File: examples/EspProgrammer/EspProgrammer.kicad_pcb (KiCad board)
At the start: 2 copper layers, 35 x 12 mm, 27 parts

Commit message: wip
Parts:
- moved UR5 10.0 mm to (137.5, 60.0), turned to -90 degrees
- moved UR4 8.08 mm to (137.5, 63.0), turned to 90 degrees
- moved UQ2 5.97 mm to (140.0, 63.0)
- moved UQ1 4.56 mm to (140.0, 60.0)
- moved UD3 3.51 mm to (152.0, 60.0)
- moved UR6 3.36 mm to (153.0, 63.0)
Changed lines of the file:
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@@
     (attr smd)
     (fp_text reference "UC4" (at 0 -1.16) (layer "F.SilkS")
-        (effects (font (size 1 1) (thickness 0.15)))
+        (effects (font (size 0.8 0.6) (thickness 0.1)))
     )
     (fp_text value "" (at 0 1.16) (layer "F.Fab")
@@
   )
   (footprint "Package_TO_SOT_SMD:SOT-323_SC-70" (layer "F.Cu")
-    (at 141.115 64.42)
+    (at 140 60)
     (descr "SOT-323, SC-70")
     (tags "SOT-323 SC-70")
@@
     (attr smd)
     (fp_text reference "UQ1" (at -0.05 -1.95) (layer "F.SilkS")
-        (effects (font (size 1 1) (thickness 0.15)))
+        (effects (font (size 0.8 0.6) (thickness 0.1)))
     )
     (fp_text value "BC847AW 1E (CBI) - 45V 200mW 100mA 110@2mA,5V 100MHz 600mV@100mA,5mA NPN +150?@(Tj) SOT-323 Bipolar Transistors - BJT ROHS" (at -0.05 2.05) (layer "F.Fab")
@@
     (attr smd)
     (fp_text reference "UR2" (at 0 -1.17 180) (layer "F.SilkS")
-        (effects (font (size 1 1) (thickness 0.15)))
+        (effects (font (size 0.8 0.6) (thickness 0.1)))
     )
     (fp_text value "" (at 0 1.17 180) (layer "F.Fab")
@@
     (property "edg_short_path" "out")
     (fp_text reference "UJ2" (at -1.27 -4.81) (layer "F.SilkS")
-        (effects (font (size 1 1) (thickness 0.15)))
+        (effects (font (size 0.8 0.6) (thickness 0.1)))
     )
     (fp_text value "PinHeader2.54 Shrouded 2x3 (Generic)" (at -1.27 4.81) (layer "F.Fab")
@@
     (attr smd)
     (fp_text reference "UR1" (at 0 -1.17 180) (layer "F.SilkS")
-        (effects (font (size 1 1) (thickness 0.15)))
+        (effects (font (size 0.8 0.6) (thickness 0.1)))
     )
     (fp_text value "" (at 0 1.17 180) (layer "F.Fab")
@@
   )
   (footprint "Resistor_SMD:R_0402_1005Metric" (layer "F.Cu")
-    (at 145.565 63.45)
+    (at 137.5 63 90)
     (descr "Resistor SMD 0402 (1005 Metric), square (rectangular) end terminal, IPC_7351 nominal, (Body size source: IPC-SM-782 page 72, https://www.pcb-3d.com/wordpress/wp-content/uploads/ipc-sm-782a_amendment_1_and_2.pdf), generated with kicad-footprint-generator")
     (tags "resistor")
@@
     (property "edg_short_path" "auto.dtr_res")
     (attr smd)
-    (fp_text reference "UR4" (at 0 -1.17) (layer "F.SilkS")
-        (effects (font (size 1 1) (thickness 0.15)))
-    )
-    (fp_text value "" (at 0 1.17) (layer "F.Fab")
-        (effects (font (size 1 1) (thickness 0.15)))
-    )
-    (fp_text user "${REFERENCE}" (at 0 0) (layer "F.Fab")
+    (fp_text reference "UR4" (at 0 -1.17 90) (layer "F.SilkS")
+        (effects (font (size 0.8 0.6) (thickness 0.1)))
+    )
+    (fp_text value "" (at 0 1.17 90) (layer "F.Fab")
+        (effects (font (size 1 1) (thickness 0.15)))
+    )
+    (fp_text user "${REFERENCE}" (at 0 0 90) (layer "F.Fab")
         (effects (font (size 0.26 0.26) (thickness 0.04)))
     )
@@
     (fp_line (start 0.525 0.27) (end -0.525 0.27)
       (stroke (width 0.1) (type solid)) (layer "F.Fab"))
-    (pad "1" smd roundrect (at -0.51 0) (size 0.54 0.64) (layers "F.Cu" "F.Paste" "F.Mask") (roundrect_rratio 0.25)
+    (pad "1" smd roundrect (at -0.51 0 90) (size 0.54 0.64) (layers "F.Cu" "F.Paste" "F.Mask") (roundrect_rratio 0.25)
       (net 13 "usbconv.dtr"))
-    (pad "2" smd roundrect (at 0.51 0) (size 0.54 0.64) (layers "F.Cu" "F.Paste" "F.Mask") (roundrect_rratio 0.25)
+    (pad "2" smd roundrect (at 0.51 0 90) (size 0.54 0.64) (layers "F.Cu" "F.Paste" "F.Mask") (roundrect_rratio 0.25)
       (net 22 "auto.dtr_res.b"))
     (model "${KICAD6_3DMODEL_DIR}/Resistor_SMD.3dshapes/R_0402_1005Metric.wrl"
@@
     (attr smd)
     (fp_text reference "UC2" (at 0 -1.16 180) (layer "F.SilkS")
-        (effects (font (size 1 1) (thickness 0.15)))
+        (effects (font (size 0.8 0.6) (thickness 0.1)))
     )
     (fp_text value "" (at 0 1.16 180) (layer "F.Fab")
@@
   )
   (footprint "LED_SMD:LED_0603_1608Metric" (layer "F.Cu")
-    (at 151.615 63.49)
+    (at 152 60)
     (descr "LED SMD 0603 (1608 Metric), square (rectangular) end terminal, IPC_7351 nominal, (Body size source: http://www.tortai-tech.com/upload/download/2011102023233369053.pdf), generated with kicad-footprint-generator")
     (tags "LED")
@@
     (attr smd)
     (fp_text reference "UD3" (at 0 -1.43) (layer "F.SilkS")
-        (effects (font (size 1 1) (thickness 0.15)))
+        (effects (font (size 0.8 0.6) (thickness 0.1)))
     )
     (fp_text value "KT-0603R (Hubei KENTO Elec) - Red 615~630nm 1.9~2.2V 0603 Light Emitting Diodes (LED) RoHS" (at 0 1.43) (layer "F.Fab")
@@
     (attr smd)
     (fp_text reference "UC1" (at 0 -1.16 180) (layer "F.SilkS")
-        (effects (font (size 1 1) (thickness 0.15)))
+        (effects (font (size 0.8 0.6) (thickness 0.1)))
     )
     (fp_text value "" (at 0 1.16 180) (layer "F.Fab")
@@
   )
   (footprint "Resistor_SMD:R_0402_1005Metric" (layer "F.Cu")
-    (at 151.575 66.04)
+    (at 153 63)
     (descr "Resistor SMD 0402 (1005 Metric), square (rectangular) end terminal, IPC_7351 nominal, (Body size source: IPC-SM-782 page 72, https://www.pcb-3d.com/wordpress/wp-content/uploads/ipc-sm-782a_amendment_1_and_2.pdf), generated with kicad-footprint-generator")
     (tags "resistor")
@@
     (attr smd)
     (fp_text reference "UR6" (at 0 -1.17) (layer "F.SilkS")
-        (effects (font (size 1 1) (thickness 0.15)))
+        (effects (font (size 0.8 0.6) (thickness 0.1)))
     )
     (fp_text value "" (at 0 1.17) (layer "F.Fab")
@@
   )
   (footprint "Package_TO_SOT_SMD:SOT-323_SC-70" (layer "F.Cu")
-    (at 141.115 68.87)
+    (at 140 63)
     (descr "SOT-323, SC-70")
     (tags "SOT-323 SC-70")
@@
     (attr smd)
     (fp_text reference "UQ2" (at -0.05 -1.95) (layer "F.SilkS")
-        (effects (font (size 1 1) (thickness 0.15)))
+        (effects (font (size 0.8 0.6) (thickness 0.1)))
     )
     (fp_text value "BC847AW 1E (CBI) - 45V 200mW 100mA 110@2mA,5V 100MHz 600mV@100mA,5mA NPN +150?@(Tj) SOT-323 Bipolar Transistors - BJT ROHS" (at -0.05 2.05) (layer "F.Fab")
@@
     (attr smd)
     (fp_text reference "UC3" (at 0 -1.16) (layer "F.SilkS")
-        (effects (font (size 1 1) (thickness 0.15)))
+        (effects (font (size 0.8 0.6) (thickness 0.1)))
     )
     (fp_text value "" (at 0 1.16) (layer "F.Fab")
@@
     (attr smd)
     (fp_text reference "UR3" (at 0 -1.17 180) (layer "F.SilkS")
-        (effects (font (size 1 1) (thickness 0.15)))
+        (effects (font (size 0.8 0.6) (thickness 0.1)))
     )
     (fp_text value "" (at 0 1.17 180) (layer "F.Fab")
@@
   )
   (footprint "Resistor_SMD:R_0402_1005Metric" (layer "F.Cu")
-    (at 145.565 65.96)
+    (at 137.5 60 -90)
     (descr "Resistor SMD 0402 (1005 Metric), square (rectangular) end terminal, IPC_7351 nominal, (Body size source: IPC-SM-782 page 72, https://www.pcb-3d.com/wordpress/wp-content/uploads/ipc-sm-782a_amendment_1_and_2.pdf), generated with kicad-footprint-generator")
     (tags "resistor")
@@
     (property "edg_short_path" "auto.rts_res")
     (attr smd)
-    (fp_text reference "UR5" (at 0 -1.17) (layer "F.SilkS")
-        (effects (font (size 1 1) (thickness 0.15)))
-    )
-    (fp_text value "" (at 0 1.17) (layer "F.Fab")
-        (effects (font (size 1 1) (thickness 0.15)))
-    )
-    (fp_text user "${REFERENCE}" (at 0 0) (layer "F.Fab")
+    (fp_text reference "UR5" (at 0 -1.17 90) (layer "F.SilkS")
+        (effects (font (size 0.8 0.6) (thickness 0.1)))
+    )
+    (fp_text value "" (at 0 1.17 90) (layer "F.Fab")
+        (effects (font (size 1 1) (thickness 0.15)))
+    )
+    (fp_text user "${REFERENCE}" (at 0 0 90) (layer "F.Fab")
         (effects (font (size 0.26 0.26) (thickness 0.04)))
     )
@@
     (fp_line (start 0.525 0.27) (end -0.525 0.27)
       (stroke (width 0.1) (type solid)) (layer "F.Fab"))
-    (pad "1" smd roundrect (at -0.51 0) (size 0.54 0.64) (layers "F.Cu" "F.Paste" "F.Mask") (roundrect_rratio 0.25)
+    (pad "1" smd roundrect (at -0.51 0 270) (size 0.54 0.64) (layers "F.Cu" "F.Paste" "F.Mask") (roundrect_rratio 0.25)
       (net 10 "usbconv.rts"))
-    (pad "2" smd roundrect (at 0.51 0) (size 0.54 0.64) (layers "F.Cu" "F.Paste" "F.Mask") (roundrect_rratio 0.25)
+    (pad "2" smd roundrect (at 0.51 0 270) (size 0.54 0.64) (layers "F.Cu" "F.Paste" "F.Mask") (roundrect_rratio 0.25)
       (net 23 "auto.rts_res.b"))
     (model "${KICAD6_3DMODEL_DIR}/Resistor_SMD.3dshapes/R_0402_1005Metric.wrl"

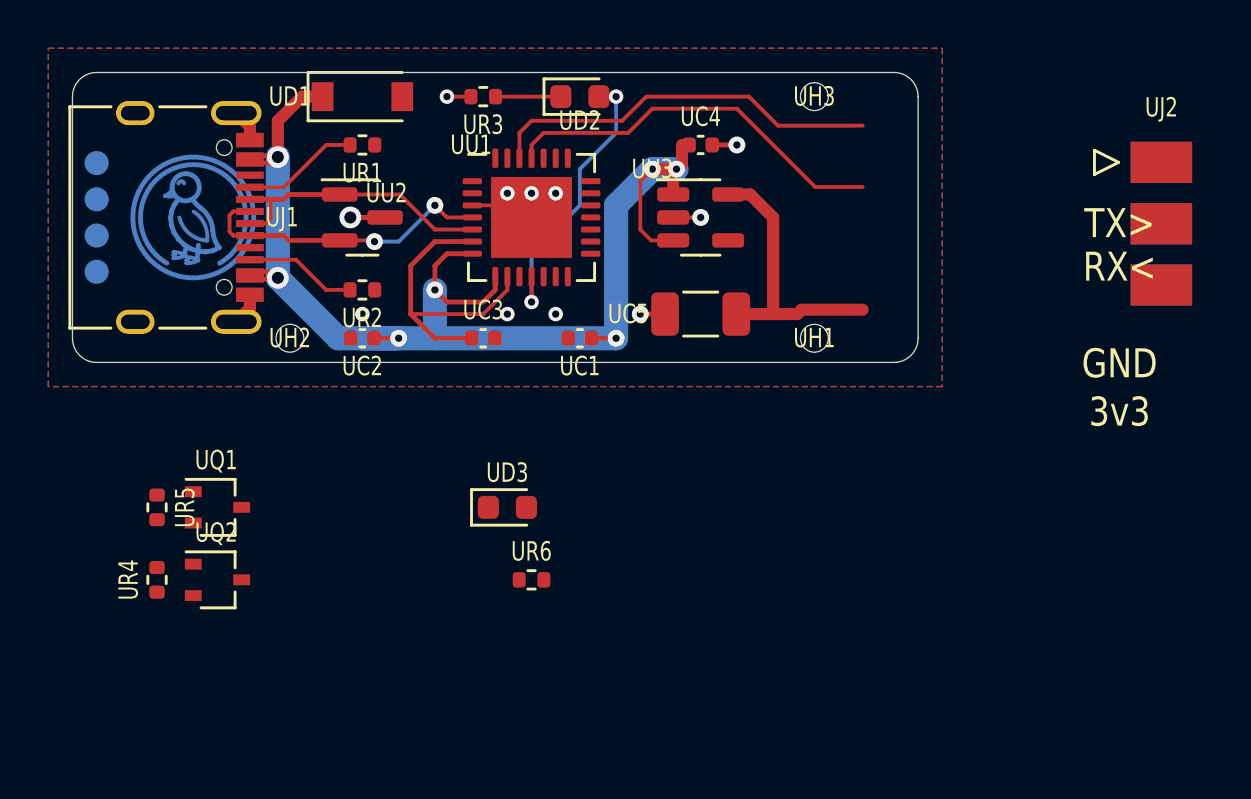
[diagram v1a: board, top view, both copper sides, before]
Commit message: exclude labels from schematic
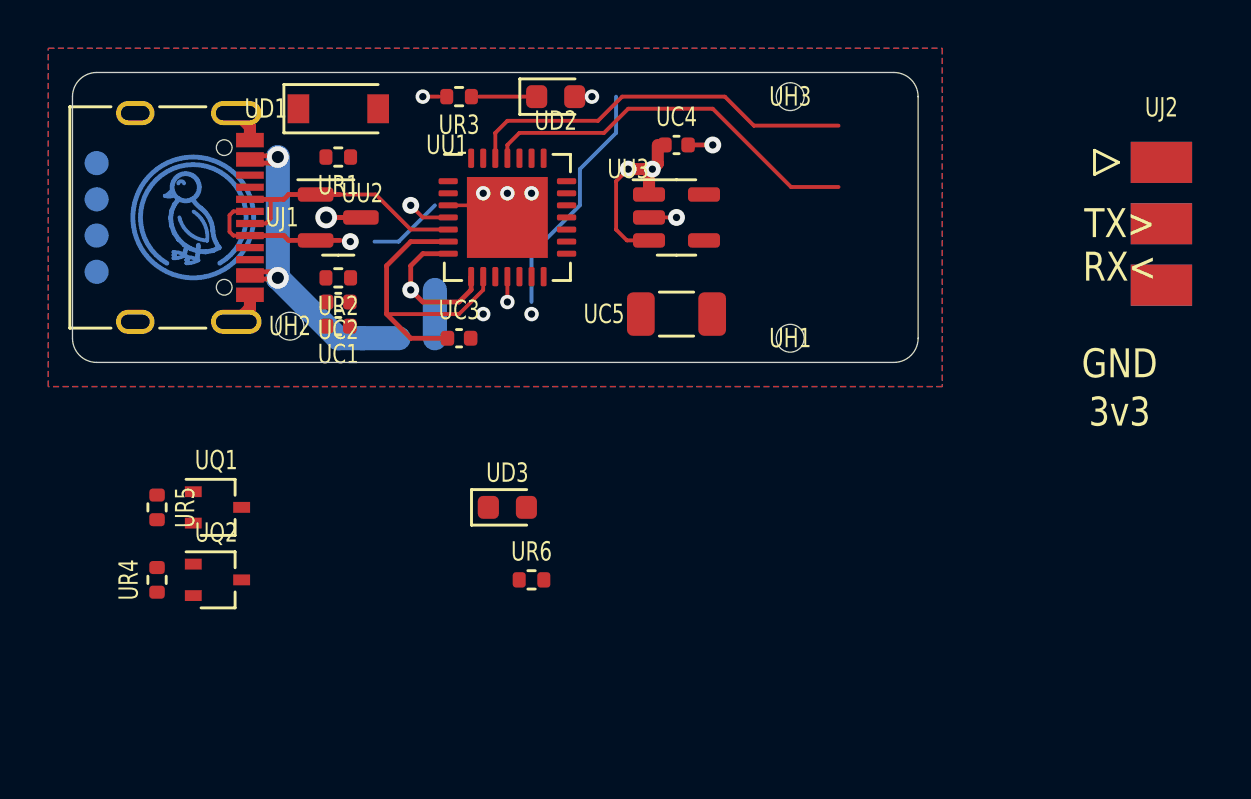
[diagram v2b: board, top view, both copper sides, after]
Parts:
- moved UC1 10.0 mm to (145.0, 52.5)
- moved UC2 1.80 mm to (145.0, 51.5)
- moved UD1 1.12 mm to (145.0, 43.5)
- moved UR1 1.12 mm to (145.0, 45.5)
- moved UR2 1.12 mm to (145.0, 50.5)
- moved UC3 1.00 mm to (150.0, 53.0)
- moved UC4 1.00 mm to (159.0, 45.0)
- moved UC5 1.00 mm to (159.0, 52.0)
- moved UD2 1.00 mm to (154.0, 43.0)
- moved UH1 1.00 mm to (163.7, 53.0)
- moved UH3 1.00 mm to (163.7, 43.0)
- moved UR3 1.00 mm to (150.0, 43.0)
- moved UU1 1.00 mm to (152.0, 48.0)
- moved UU2 1.00 mm to (145.0, 48.0)
- moved UU3 1.00 mm to (159.0, 48.0)
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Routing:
- net vusb: track 54.4 -> 30.2 mm, vias 7 -> 5
- net v3v3: track 11.6 -> 0.00 mm
- net usb_uart.conn.A5: track 4.23 -> 0.00 mm
- net usb_uart.conn.B5: track 4.02 -> 0.00 mm
- net gnd: track 11.5 -> 10.5 mm, vias 11 -> 9

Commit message: vague floorplan
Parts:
- UC5: footprint Capacitor_SMD:C_1206_3216Metric -> Capacitor_SMD:C_0805_2012Metric
- moved UQ2 25.5 mm to (161.0, 48.5)
- moved UR4 24.0 mm to (157.0, 49.0), turned to 180 degrees
- moved UR5 22.9 mm to (157.0, 48.0), turned to 180 degrees
- moved UQ1 22.7 mm to (161.0, 51.5)
- moved UJ2 13.8 mm to (166.5, 48.0)
- moved UR6 10.5 mm to (153.5, 52.5), turned to 180 degrees
- moved UH1 9.59 mm to (165.0, 43.5)
- moved UH3 9.59 mm to (165.0, 52.5)
- moved UR3 9.55 mm to (151.0, 52.5)
- moved UD3 9.43 mm to (157.0, 52.0)
- moved UD2 8.08 mm to (157.0, 50.5)
- moved UC5 7.76 mm to (161.0, 44.5), turned to 0 degrees
- moved UC4 5.59 mm to (153.5, 44.0), turned to 180 degrees
- moved UU3 3.61 mm to (157.0, 45.0)
- moved UC3 1.58 mm to (148.5, 52.5)
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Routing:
- net usbconv.uart.rx: track 16.2 -> 1.26 mm
- net usbconv.uart.tx: track 16.4 -> 1.76 mm
- net usbconv.nsuspend: track 11.7 -> 1.05 mm, vias 2 -> 1
- net vusb: track 30.2 -> 20.8 mm, vias 5 -> 3
- net usbconv.ic.vdd: track 12.6 -> 3.51 mm
- net gnd: track 10.5 -> 7.94 mm, vias 9 -> 4
- net led.res.a: track 2.39 -> 0.00 mm
- net usb_chain_0.d_N: track 12.4 -> 11.4 mm
- net usb_chain_0.d_P: track 13.0 -> 13.5 mm

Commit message: d e n s i t y
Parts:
- moved UC2 3.64 mm to (148.5, 52.5), turned to 0 degrees
- moved UC3 3.64 mm to (145.0, 51.5), turned to 180 degrees
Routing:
- net usbconv.ic.vdd: track 3.51 -> 10.6 mm, vias 0 -> 2
- net gnd: track 7.94 -> 12.5 mm, vias 4 -> 9
- net usb_uart.conn.A5: track 0.00 -> 3.56 mm
- net usb_uart.conn.B5: track 0.00 -> 3.35 mm
- net usb_chain_0.d_P: track 13.5 -> 12.7 mm

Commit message: layout complete
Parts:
- turned UR4 to 0 degrees
- turned UR5 to 0 degrees
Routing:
- net usbconv.rts: track 0.00 -> 24.2 mm, vias 0 -> 3
- net vusb: track 20.3 -> 43.8 mm, vias 3 -> 4
- net v3v3: track 0.00 -> 18.9 mm
- net usbconv.uart.tx: track 1.76 -> 18.8 mm, vias 0 -> 1
- net usbconv.dtr: track 0.00 -> 16.3 mm, vias 0 -> 3
- net usbconv.uart.rx: track 1.26 -> 17.1 mm, vias 0 -> 2
- net usbconv.nsuspend: track 1.05 -> 10.5 mm, vias 1 -> 2
- net led.res.a: track 0.00 -> 5.83 mm
- net gnd: track 12.5 -> 18.1 mm, vias 9 -> 10
- net auto.boot: track 0.00 -> 5.37 mm, vias 0 -> 1
- net auto.en: track 0.00 -> 4.63 mm, vias 0 -> 1
- net auto.dtr_res.b: track 0.00 -> 3.46 mm
- net auto.rts_res.b: track 0.00 -> 2.55 mm
- net led_en.res.a: track 0.00 -> 2.41 mm
- net usbconv.ic.vdd: track 10.6 -> 9.72 mm
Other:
- board size 35 x 12 mm -> 32.5 x 11 mm
- board text removed: "3v3"
- board text removed: "GND"
- board text removed: "RX<"
- board text removed: "TX>"

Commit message: wip kinda done
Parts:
- moved UC5 0.50 mm to (161.0, 45.0)
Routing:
- net v3v3: track 18.9 -> 22.6 mm
- net vusb: track 43.8 -> 45.1 mm
- net auto.en: track 4.63 -> 3.53 mm
- net usbconv.dtr: track 16.3 -> 15.2 mm
- net gnd: track 18.1 -> 19.2 mm
- net usbconv.ic.vdd: track 9.72 -> 8.80 mm
- net usbconv.rts: track 24.2 -> 24.8 mm
- net usbconv.uart.tx: track 18.8 -> 18.3 mm
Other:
- board text added: "CP2102 ESP32 Pgm May '23"
- board text removed: "CP2102 USB-UART Jan '23"

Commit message: cleaning
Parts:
- UD1: value MMSZ5232A_R1_00001 (PANJIT International) - 5?A@3V 11? Single 5.49V~5.71V 500mW 5.6V SOD-123 Zener Diodes ROHS -> BZT52-B5V6S_R1_00001 (PANJIT International) - 100nA@1V 40? Single 5.49V~5.71V 200mW 5.6V SOD-323 Zener Diodes ROHS; footprint Diode_SMD:D_SOD-123 -> Diode_SMD:D_SOD-323
- moved UH1 1.55 mm to (163.5, 43.9)
- moved UH3 1.55 mm to (163.5, 52.1)
- moved UU4 0.58 mm to (138.4, 48.0)
- moved UH2 0.38 mm to (143.0, 52.1)
- turned UC5 to 180 degrees
- renumbered UR4 to UR3, UR5 to UR4, UR3 to UR5
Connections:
- UD2 pad 2: usbconv.nsuspend -> v3v3
- UR5 pad 2: gnd -> usbconv.suspend
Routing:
- net usbconv.nsuspend: track 10.5 -> 0.00 mm, vias 2 -> 0
- net usbconv.uart.tx: track 18.3 -> 21.0 mm
- net usbconv.suspend: track 0.00 -> 2.47 mm
- net gnd: track 19.2 -> 17.4 mm, vias 10 -> 8
- net usbconv.dtr: track 15.2 -> 16.6 mm
- net usbconv.rts: track 24.8 -> 23.7 mm
- net usbconv.uart.rx: track 17.2 -> 18.2 mm
- net auto.en: track 3.53 -> 4.53 mm
- net v3v3: track 22.6 -> 21.7 mm
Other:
- board size 32.5 x 11 mm -> 32.5 x 10 mm

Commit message: layout cleanups
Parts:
- UQ1, UQ2: value BC847AW 1E (CBI) - 45V 200mW 100mA 110@2mA,5V 100MHz 600mV@100mA,5mA NPN +150?@(Tj) SOT-323 Bipolar Transistors - BJT R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 -> BC846BW 1B (CBI) - 65V 330mW 100mA 290@2mA,5V 250MHz 200mV@100mA,5mA NPN +150?@(Tj) SOT-323-3 Bipolar Transistors - BJT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
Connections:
- net auto.boot renamed Uauto.boot
- net auto.dtr_res.b renamed Uauto.dtr_res.b
- net auto.en renamed Uauto.en
- net auto.rts_res.b renamed Uauto.rts_res.b
- net gnd renamed Ugnd
- net led.res.a renamed Uled.res.a
- net led_en.res.a renamed Uled_en.res.a
- net usb_chain_0.d_N renamed Uusb_chain_0.d_N
- net usb_chain_0.d_P renamed Uusb_chain_0.d_P
- net usb_uart.conn.A5 renamed Uusb_uart.conn.A5
- net usb_uart.conn.B5 renamed Uusb_uart.conn.B5
- net usbconv.cts renamed Uusbconv.cts
- net usbconv.dcd renamed Uusbconv.dcd
- net usbconv.dsr renamed Uusbconv.dsr
- net usbconv.dtr renamed Uusbconv.dtr
- net usbconv.ic.vdd renamed Uusbconv.ic.vdd
- net usbconv.nsuspend renamed Uusbconv.nsuspend
- net usbconv.ri renamed Uusbconv.ri
- net usbconv.rts renamed Uusbconv.rts
- net usbconv.suspend renamed Uusbconv.suspend
- net usbconv.uart.rx renamed Uusbconv.uart.rx
- net usbconv.uart.tx renamed Uusbconv.uart.tx
- net v3v3 renamed Uv3v3
- net vusb renamed Uvusb
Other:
- board text added: "CP2102 ESP32 Pgm Oct '23"
- board text removed: "CP2102 ESP32 Pgm May '23"
